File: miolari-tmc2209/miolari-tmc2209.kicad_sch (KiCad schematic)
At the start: 32 parts, among them J1 Spread, J2 MS1, J3 MS2, J4 TMC2209_Conn, J5 DriverConn, J9 TMC2209_VIN, U2 TMC2209-LA

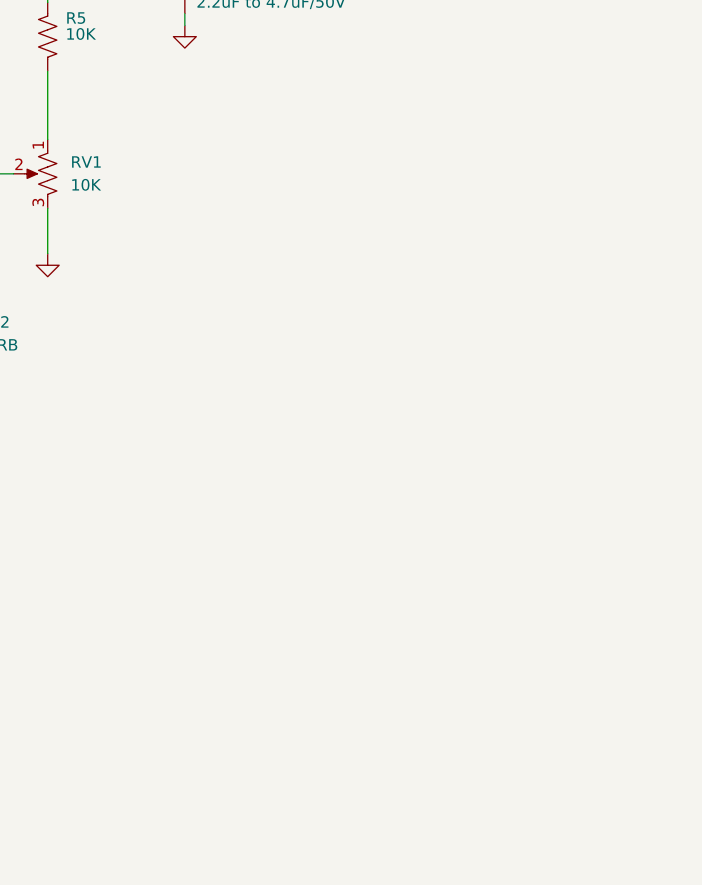
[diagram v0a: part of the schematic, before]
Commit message: add idc connector to miolari tmc2209
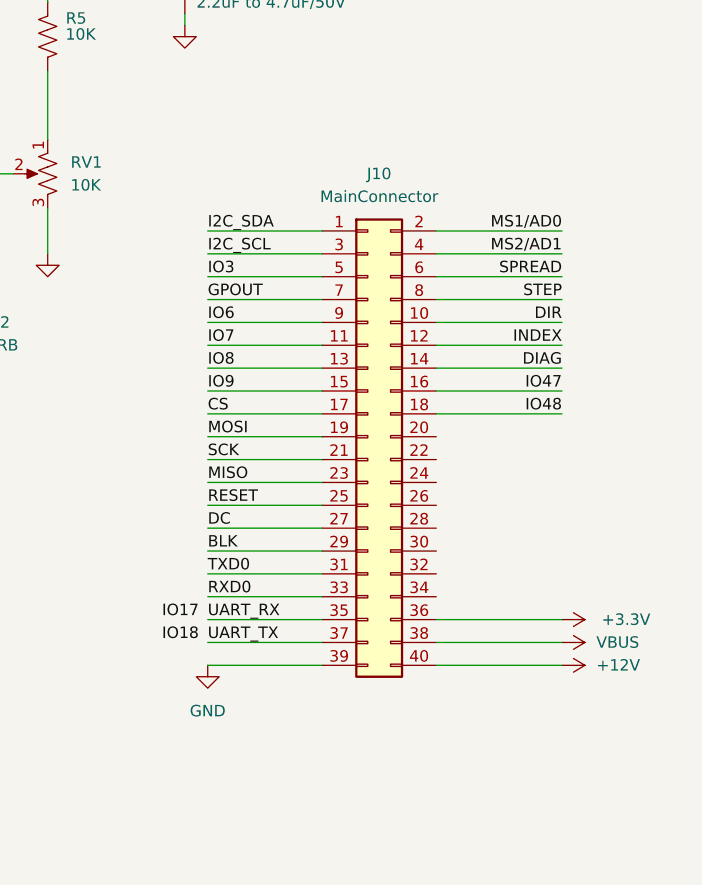
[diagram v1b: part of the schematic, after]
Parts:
- added J10: MainConnector, Connector_IDC:IDC-Header_2x20_P2.54mm_Vertical, symbol Connector_Generic:Conn_02x20_Odd_Even
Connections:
- net +3.3V: now also J10.36 (Pin_36)
- net DIAG: now also J10.14 (Pin_14)
- net DIR: now also J10.10 (Pin_10)
- net GND: now also J10.39 (Pin_39)
- net INDEX: now also J10.12 (Pin_12)
- net MS1/AD0: now also J10.2 (Pin_2)
- net MS2/AD1: now also J10.4 (Pin_4)
- net SPREAD: now also J10.6 (Pin_6)
- net STEP: now also J10.8 (Pin_8)
- net UART_RX: now also J10.35 (Pin_35)
- net UART_TX: now also J10.37 (Pin_37)
- new net +12V: J10.40 (Pin_40)
- new net BLK: J10.29 (Pin_29)
- new net CS: J10.17 (Pin_17)
- new net DC: J10.27 (Pin_27)
- new net GPOUT: J10.7 (Pin_7)
- new net I2C_SCL: J10.3 (Pin_3)
- new net I2C_SDA: J10.1 (Pin_1)
- new net IO3: J10.5 (Pin_5)
- new net IO47: J10.16 (Pin_16)
- new net IO48: J10.18 (Pin_18)
- new net IO6: J10.9 (Pin_9)
- new net IO7: J10.11 (Pin_11)
- new net IO8: J10.13 (Pin_13)
- new net IO9: J10.15 (Pin_15)
- new net MISO: J10.23 (Pin_23)
- new net MOSI: J10.19 (Pin_19)
- new net RESET: J10.25 (Pin_25)
- new net RXD0: J10.33 (Pin_33)
- new net SCK: J10.21 (Pin_21)
- new net TXD0: J10.31 (Pin_31)
- new net VBUS: J10.38 (Pin_38)

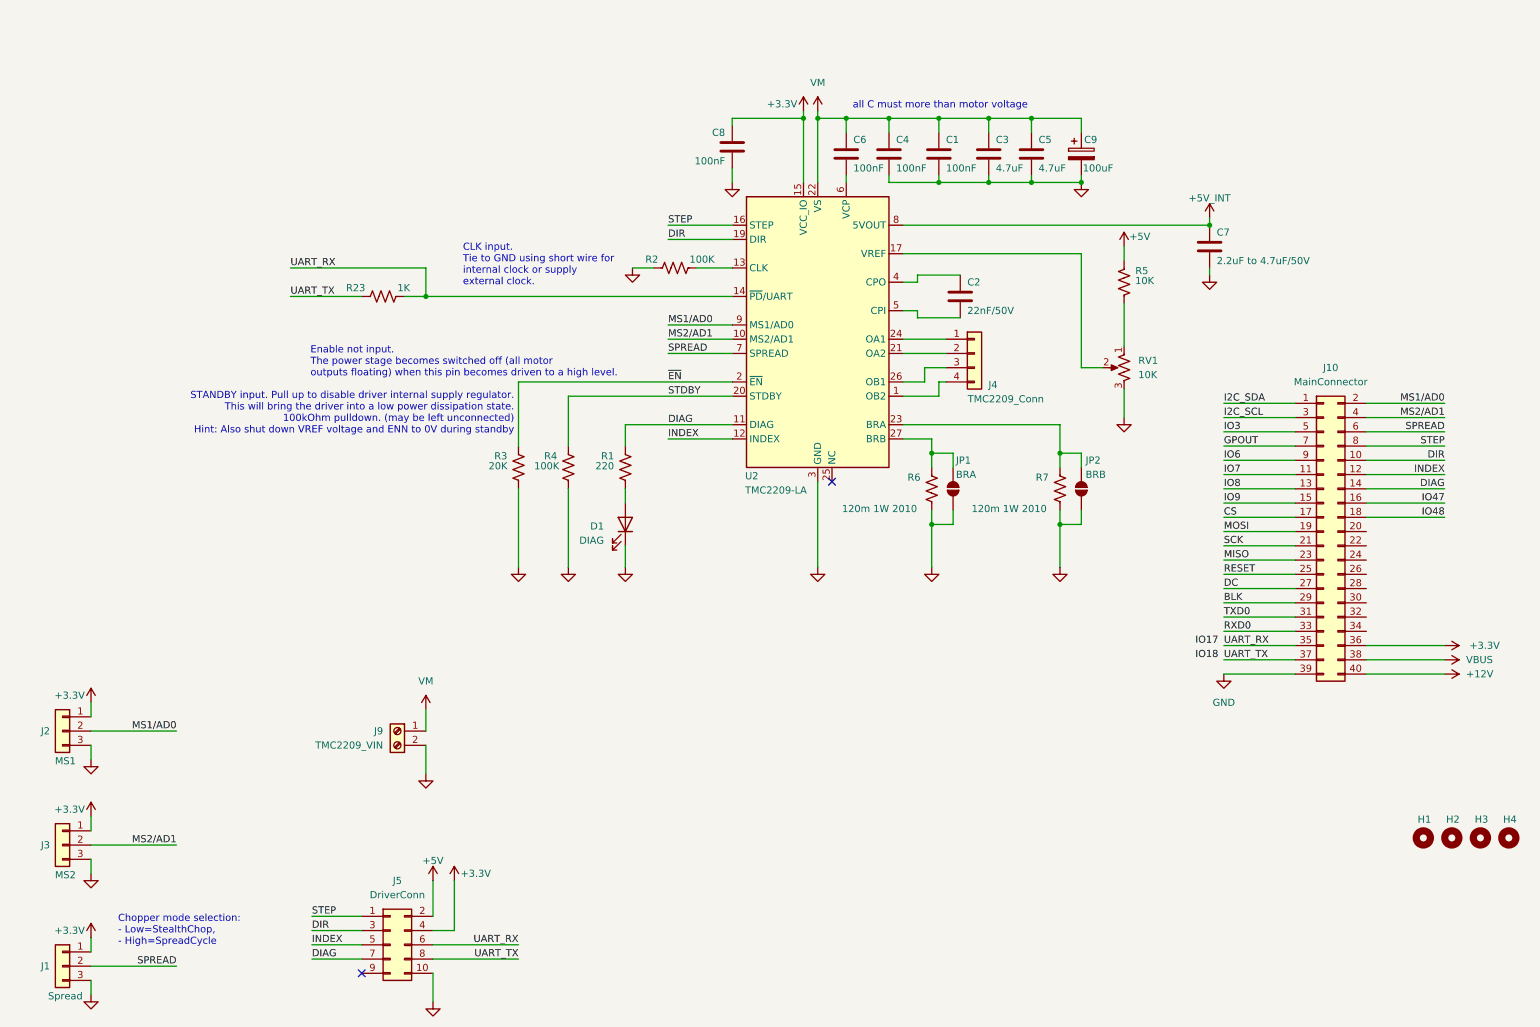
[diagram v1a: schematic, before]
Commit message: finish un-tidy miolari tmc2209
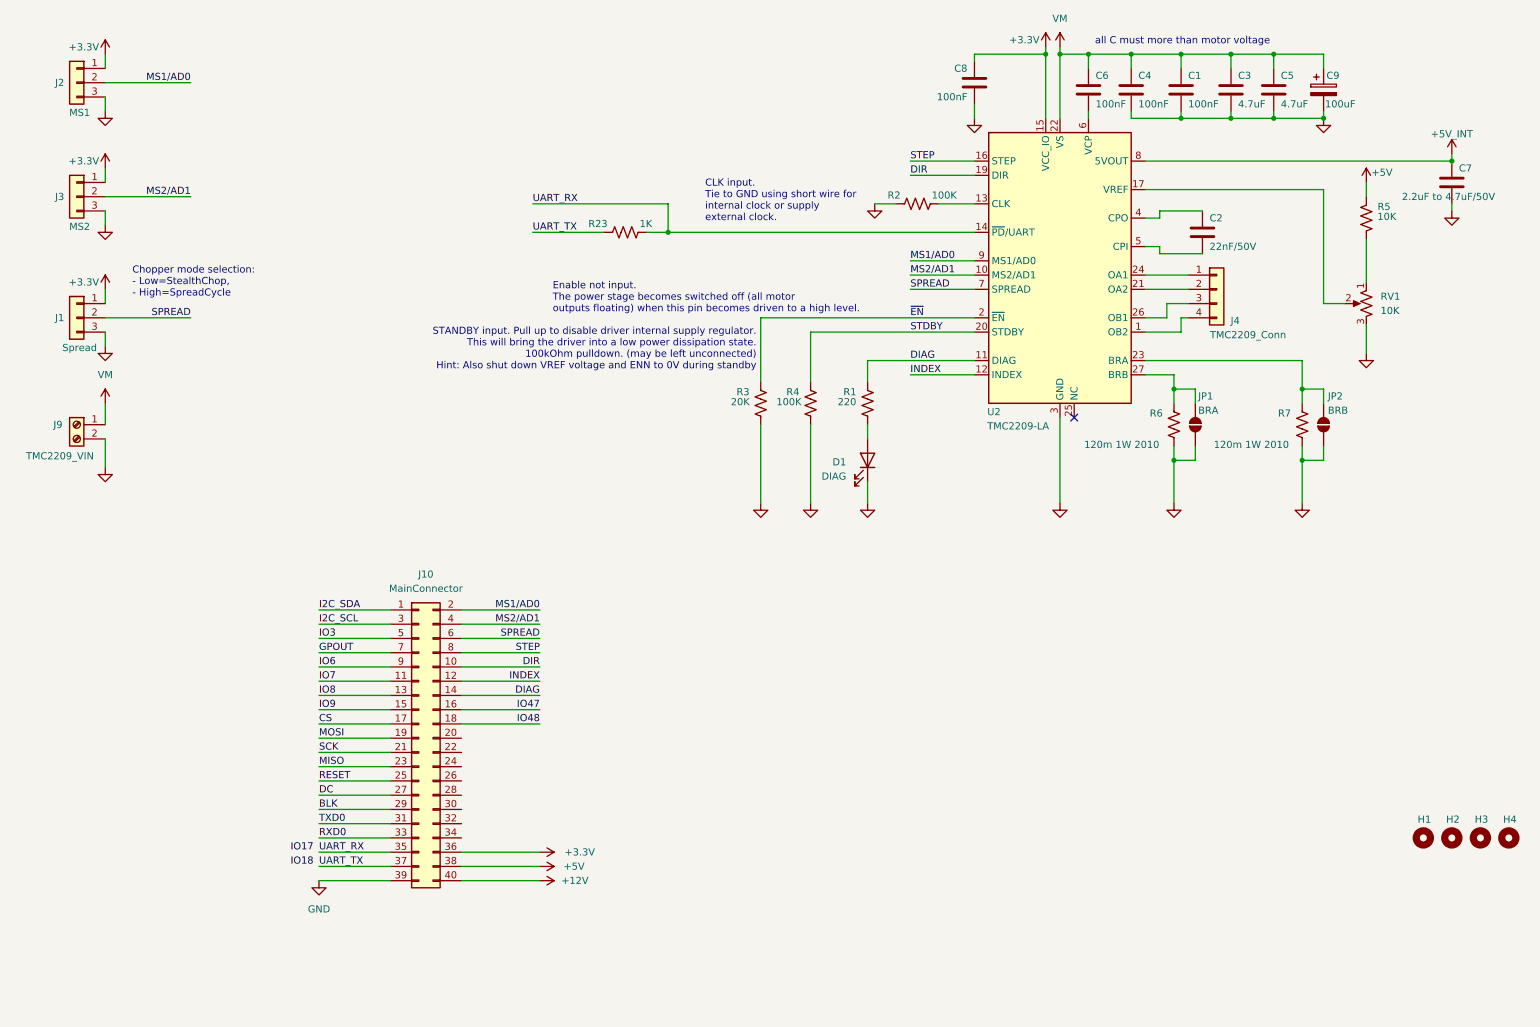
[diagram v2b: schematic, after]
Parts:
- removed J5: DriverConn, Connector_IDC:IDC-Header_2x05_P2.54mm_Vertical, symbol Connector_Generic:Conn_02x05_Odd_Even
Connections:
- net VBUS is gone; now on net +5V: J10.38 (Pin_38)
- no-connect marks 2 -> 1
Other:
- moved on the sheet: C1, C2, C3, C4, C5, C6, C7, C8, C9, D1, J1, J10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
